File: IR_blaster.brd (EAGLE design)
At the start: 97.8 x 82.5 mm, 54 parts, among them J2 Micro USB, J3 Mini USB, J4 nRF24L01+, J5 FTDI, Q1IL1 BC337, Q1IL2 BC337, Q1IL3 BC337, Q1IL4 BC337, SW1P SPDT_SWITCH_2MM

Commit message: Changed the batteries packages to double pin ones.
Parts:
- BATT1, BATT2: device battery:CR2032H -> SparkFun-Batteries:BATTCOM_20MM_PTH
- moved R2IL4 6.35 mm to (2.54, 59.7)
- moved R1IL4 2.84 mm to (30.5, 52.7)
- moved Q1IL4 2.84 mm to (22.2, 52.7)
- moved R1BATT 1.80 mm to (45.7, 52.7)
- moved R2BATT 1.80 mm to (38.1, 52.7)
- moved BATT1 1.80 mm to (15.2, 68.6), turned to 90 degrees
- moved BATT2 1.27 mm to (38.1, 68.6), turned to 90 degrees
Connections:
- net GND: now also BATT1.2, BATT2.2; no longer BATT1.-, BATT2.-
- net V_BATT: now also BATT1.1, BATT2.1; no longer BATT1.+, BATT2.+
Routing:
- net N$15: track 9.94 -> 16.3 mm
- net 10: track 35.3 -> 39.0 mm
- net A0: track 14.4 -> 12.1 mm
- net N$14: track 33.2 -> 31.1 mm
- net V_BATT: track 109.3 -> 111.3 mm
- net N$16: track 8.67 -> 7.93 mm
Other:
- board text added: "revision 1.1"
- board text removed: "v"

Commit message: ...
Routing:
- net GND: track 18.2 -> 210.3 mm, vias 1 -> 8
- net CE: track 55.1 -> 61.4 mm
- net N$14: track 31.1 -> 36.3 mm
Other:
- board text removed: "revision 1.0"
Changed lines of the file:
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@@
 <wire x1="74.93" y1="10.16" x2="90.17" y2="10.16" width="0.254" layer="21"/>
 <wire x1="90.17" y1="10.16" x2="90.17" y2="38.1" width="0.254" layer="21"/>
-<text x="16.51" y="1.905" size="3.5" layer="1" font="vector">IR blaster</text>
-<text x="16.51" y="1.905" size="3.5" layer="31" font="vector">IR blaster</text>
-<text x="44.45" y="1.905" size="3.5" layer="16" font="vector" rot="MR0">IR blaster</text>
-<text x="32.385" y="5.08" size="1.27" layer="1" font="vector">revision 1.0</text>
-<text x="32.385" y="5.08" size="1.27" layer="31" font="vector">revision 1.1</text>
-<text x="28.575" y="5.08" size="1.27" layer="16" font="vector" rot="MR0">revision 1.1</text>
+<text x="17.78" y="2.54" size="3" layer="1" font="vector">IR blaster</text>
+<text x="17.78" y="2.54" size="3" layer="31" font="vector">IR blaster</text>
+<text x="41.91" y="2.54" size="3" layer="16" font="vector" rot="MR0">IR blaster</text>
+<text x="29.21" y="5.08" size="1.27" layer="1" font="vector">revision 1.1</text>
+<text x="29.21" y="5.08" size="1.27" layer="31" font="vector">revision 1.1</text>
+<text x="30.48" y="5.08" size="1.27" layer="16" font="vector" rot="MR0">revision 1.1</text>
 <text x="40.64" y="67.945" size="3.81" layer="16" font="vector" rot="MR0">Batteries</text>
 <text x="60.96" y="39.37" size="1.9304" layer="16" font="vector" rot="MR0">Microcontroller</text>
@@
 <text x="39.37" y="39.37" size="2.54" layer="31" font="vector">ATmega328</text>
 <text x="78.74" y="38.735" size="1.4224" layer="1" font="vector">nRF24L01+</text>
-<text x="22.86" y="59.69" size="1.778" layer="1" font="vector">CR2032</text>
-<text x="22.86" y="59.69" size="1.778" layer="31" font="vector">CR2032</text>
+<text x="22.225" y="58.42" size="1.778" layer="1" font="vector">CR2032</text>
+<text x="22.225" y="58.42" size="1.778" layer="31" font="vector">CR2032</text>
 <text x="22.225" y="34.29" size="1.4224" layer="31" font="vector">Restart</text>
 <text x="22.225" y="34.29" size="1.4224" layer="1" font="vector">Restart</text>
@@
 <via x="64.135" y="76.835" extent="1-16" drill="1" shape="square"/>
 <wire x1="64.135" y1="76.835" x2="66.04" y2="76.835" width="0.8128" layer="1"/>
+<wire x1="15.24" y1="60.43" x2="15.77" y2="60.43" width="1.27" layer="16"/>
+<wire x1="15.77" y1="60.43" x2="16.51" y2="59.69" width="1.27" layer="16"/>
+<wire x1="16.51" y1="59.69" x2="16.51" y2="55.88" width="1.27" layer="16"/>
+<wire x1="38.1" y1="60.43" x2="38.1" y2="56.515" width="1.27" layer="16"/>
+<wire x1="6.985" y1="46.99" x2="6.985" y2="48.26" width="0.8128" layer="16"/>
+<wire x1="6.985" y1="48.26" x2="7.62" y2="48.895" width="0.8128" layer="16"/>
+<wire x1="7.62" y1="48.895" x2="14.605" y2="48.895" width="0.8128" layer="16"/>
+<wire x1="14.605" y1="48.895" x2="16.51" y2="50.8" width="0.8128" layer="16"/>
+<wire x1="16.51" y1="50.8" x2="16.51" y2="55.88" width="0.8128" layer="16"/>
+<wire x1="22.225" y1="51.435" x2="17.145" y2="51.435" width="0.8128" layer="16"/>
+<wire x1="17.145" y1="51.435" x2="16.51" y2="50.8" width="0.8128" layer="16"/>
+<wire x1="6.985" y1="54.61" x2="6.985" y2="57.785" width="1.27" layer="16"/>
+<wire x1="6.985" y1="57.785" x2="9.525" y2="60.325" width="1.27" layer="16"/>
+<wire x1="9.525" y1="60.325" x2="15.135" y2="60.325" width="1.27" layer="16"/>
+<wire x1="15.135" y1="60.325" x2="15.24" y2="60.43" width="1.27" layer="16"/>
+<wire x1="59.055" y1="59.69" x2="59.055" y2="74.295" width="0.8128" layer="16"/>
+<wire x1="80.01" y1="64.77" x2="78.74" y2="64.77" width="0.8128" layer="16"/>
+<wire x1="78.74" y1="64.77" x2="77.47" y2="63.5" width="0.8128" layer="16"/>
+<wire x1="77.47" y1="63.5" x2="73.66" y2="63.5" width="0.8128" layer="16"/>
+<wire x1="73.66" y1="63.5" x2="71.12" y2="63.5" width="0.8128" layer="16"/>
+<via x="71.12" y="63.5" extent="1-16" drill="1" shape="square"/>
+<wire x1="72.39" y1="44.45" x2="74.93" y2="41.91" width="0.8128" layer="16"/>
+<wire x1="74.93" y1="41.91" x2="81.28" y2="41.91" width="0.8128" layer="16"/>
+<via x="81.28" y="41.91" extent="1-16" drill="1" shape="square"/>
+<wire x1="48.26" y1="44.45" x2="48.26" y2="46.99" width="0.8128" layer="16"/>
+<wire x1="48.26" y1="46.99" x2="59.055" y2="57.785" width="0.8128" layer="16"/>
+<wire x1="59.055" y1="57.785" x2="59.055" y2="59.69" width="0.8128" layer="16"/>
+<wire x1="50.8" y1="36.83" x2="50.8" y2="40.64" width="0.8128" layer="16"/>
+<wire x1="50.8" y1="40.64" x2="48.26" y2="43.18" width="0.8128" layer="16"/>
+<wire x1="48.26" y1="43.18" x2="48.26" y2="44.45" width="0.8128" layer="16"/>
+<wire x1="53.34" y1="22.86" x2="57.15" y2="22.86" width="0.8128" layer="16"/>
+<via x="57.15" y="22.86" extent="1-16" drill="1" shape="square"/>
+<wire x1="77.47" y1="11.43" x2="77.47" y2="6.35" width="0.8128" layer="16"/>
+<wire x1="88.9" y1="36.83" x2="92.075" y2="36.83" width="0.8128" layer="16"/>
+<wire x1="88.9" y1="36.83" x2="88.9" y2="38.1" width="0.8128" layer="16"/>
+<wire x1="88.9" y1="38.1" x2="90.805" y2="40.005" width="0.8128" layer="16"/>
+<via x="90.805" y="40.005" extent="1-16" drill="1" shape="square"/>
+<wire x1="90.805" y1="40.005" x2="90.805" y2="41.275" width="0.8128" layer="1"/>
+<wire x1="90.805" y1="41.275" x2="90.17" y2="41.91" width="0.8128" layer="1"/>
+<wire x1="90.17" y1="41.91" x2="81.28" y2="41.91" width="0.8128" layer="1"/>
+<wire x1="55.7784" y1="10.2108" x2="55.7784" y2="4.9784" width="0.8128" layer="16"/>
+<wire x1="55.7784" y1="4.9784" x2="53.34" y2="2.54" width="0.8128" layer="16"/>
+<wire x1="53.34" y1="2.54" x2="50.8" y2="2.54" width="0.8128" layer="16"/>
+<wire x1="43.2816" y1="10.2108" x2="38.1508" y2="10.2108" width="0.8128" layer="16"/>
+<wire x1="38.1508" y1="10.2108" x2="38.1" y2="10.16" width="0.8128" layer="16"/>
+<wire x1="55.7784" y1="10.2108" x2="58.3692" y2="10.2108" width="0.8128" layer="16"/>
+<wire x1="58.3692" y1="10.2108" x2="59.69" y2="8.89" width="0.8128" layer="16"/>
+<via x="38.1" y="10.16" extent="1-16" drill="1" shape="square"/>
+<via x="59.69" y="8.89" extent="1-16" drill="1" shape="square"/>
+<wire x1="17.78" y1="11.43" x2="22.86" y2="11.43" width="0.8128" layer="16"/>
+<via x="22.86" y="11.43" extent="1-16" drill="1" shape="square"/>
+<wire x1="6.35" y1="27.94" x2="4.445" y2="27.94" width="0.8128" layer="16"/>
+<wire x1="4.445" y1="27.94" x2="3.175" y2="26.67" width="0.8128" layer="16"/>
+<wire x1="3.175" y1="26.67" x2="3.175" y2="22.225" width="0.8128" layer="16"/>
+<wire x1="3.175" y1="22.225" x2="6.35" y2="19.05" width="0.8128" layer="16"/>
+<wire x1="6.35" y1="19.05" x2="8.89" y2="19.05" width="0.8128" layer="16"/>
+<wire x1="8.89" y1="19.05" x2="10.16" y2="20.32" width="0.8128" layer="16"/>
+<wire x1="10.16" y1="20.32" x2="13.97" y2="20.32" width="0.8128" layer="16"/>
+<wire x1="13.97" y1="20.32" x2="15.24" y2="19.05" width="0.8128" layer="16"/>
+<wire x1="15.24" y1="19.05" x2="15.24" y2="12.7" width="0.8128" layer="16"/>
+<wire x1="15.24" y1="12.7" x2="16.51" y2="11.43" width="0.8128" layer="16"/>
+<wire x1="16.51" y1="11.43" x2="17.78" y2="11.43" width="0.8128" layer="16"/>
 </signal>
 <signal name="V_BATT">
@@
 <contactref element="UC" pad="13"/>
 <contactref element="J4" pad="3"/>
-<wire x1="86.36" y1="36.83" x2="86.36" y2="38.1" width="0.8128" layer="16"/>
-<wire x1="86.36" y1="38.1" x2="87.63" y2="39.37" width="0.8128" layer="16"/>
-<wire x1="87.63" y1="39.37" x2="93.98" y2="39.37" width="0.8128" layer="16"/>
-<wire x1="93.98" y1="39.37" x2="95.25" y2="38.1" width="0.8128" layer="16"/>
-<wire x1="95.25" y1="38.1" x2="95.25" y2="33.02" width="0.8128" layer="16"/>
 <wire x1="95.25" y1="33.02" x2="93.98" y2="31.75" width="0.8128" layer="16"/>
 <wire x1="93.98" y1="31.75" x2="88.9" y2="31.75" width="0.8128" layer="16"/>
@@
 <wire x1="64.135" y1="34.925" x2="63.5" y2="35.56" width="0.8128" layer="16"/>
 <wire x1="63.5" y1="35.56" x2="63.5" y2="36.83" width="0.8128" layer="16"/>
+<wire x1="86.36" y1="36.83" x2="86.36" y2="41.275" width="0.8128" layer="16"/>
+<wire x1="86.36" y1="41.275" x2="87.63" y2="42.545" width="0.8128" layer="16"/>
+<wire x1="87.63" y1="42.545" x2="93.98" y2="42.545" width="0.8128" layer="16"/>
+<wire x1="93.98" y1="42.545" x2="95.25" y2="41.275" width="0.8128" layer="16"/>
+<wire x1="95.25" y1="41.275" x2="95.25" y2="33.02" width="0.8128" layer="16"/>
 </signal>
 <signal name="2">
@@
 <contactref element="IL4" pad="K"/>
 <wire x1="22.225" y1="53.975" x2="22.225" y2="60.324996875" width="1.27" layer="16"/>
-<wire x1="22.225" y1="60.324996875" x2="4.708025" y2="77.841971875" width="1.27" layer="16"/>
+<wire x1="4.708025" y1="77.841971875" x2="4.708025" y2="68.951975" width="0.8128" layer="16"/>
+<wire x1="4.708025" y1="68.951975" x2="8.89" y2="64.77" width="0.8128" layer="16"/>
+<wire x1="8.89" y1="64.77" x2="17.779996875" y2="64.77" width="0.8128" layer="16"/>
+<wire x1="17.779996875" y1="64.77" x2="22.225" y2="60.324996875" width="0.8128" layer="16"/>
 </signal>
 <signal name="N$15">
@@
 <wire x1="43.18" y1="15.2908" x2="43.2816" y2="15.1892" width="0.8128" layer="16"/>
 </signal>
+<signal name="N$3">
+</signal>
+<signal name="N$18">
+<via x="77.47" y="6.35" extent="1-16" drill="1" shape="square"/>
+</signal>
 </signals>

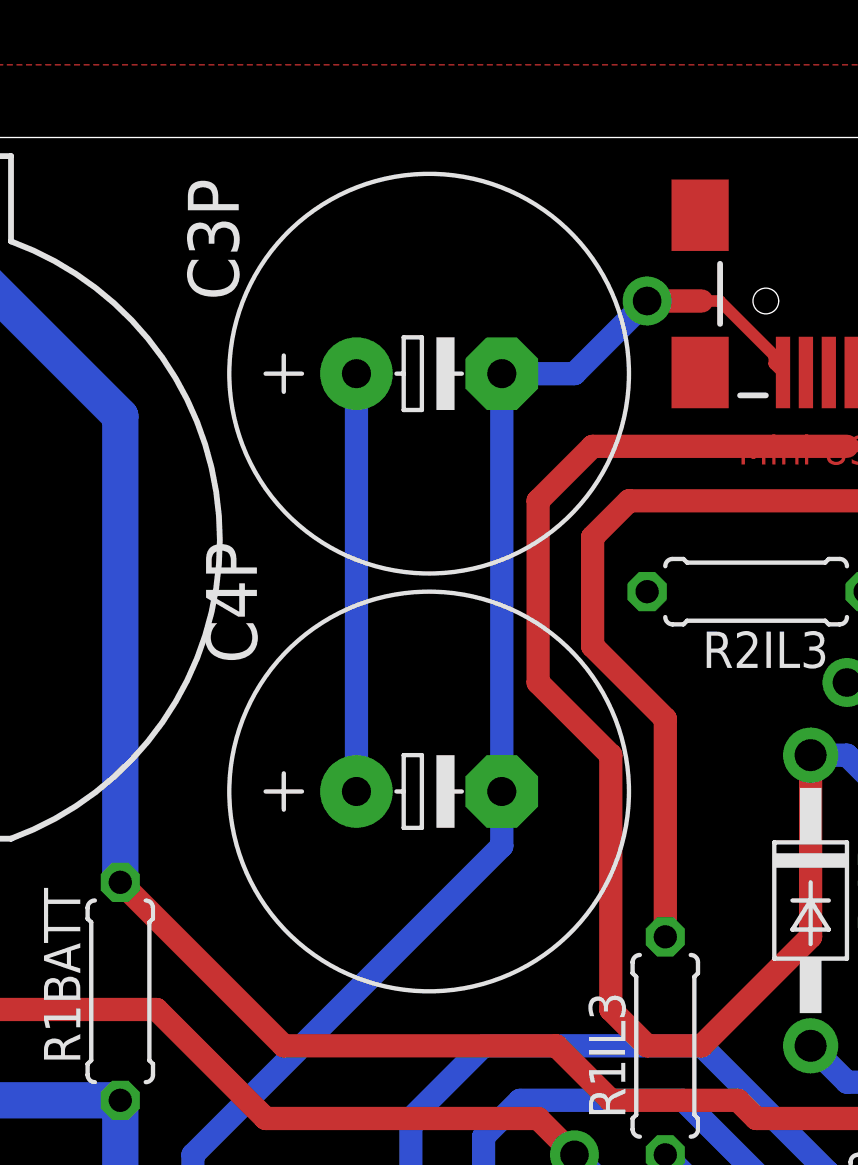
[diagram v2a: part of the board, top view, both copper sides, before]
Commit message: Changed to smaller capacitors
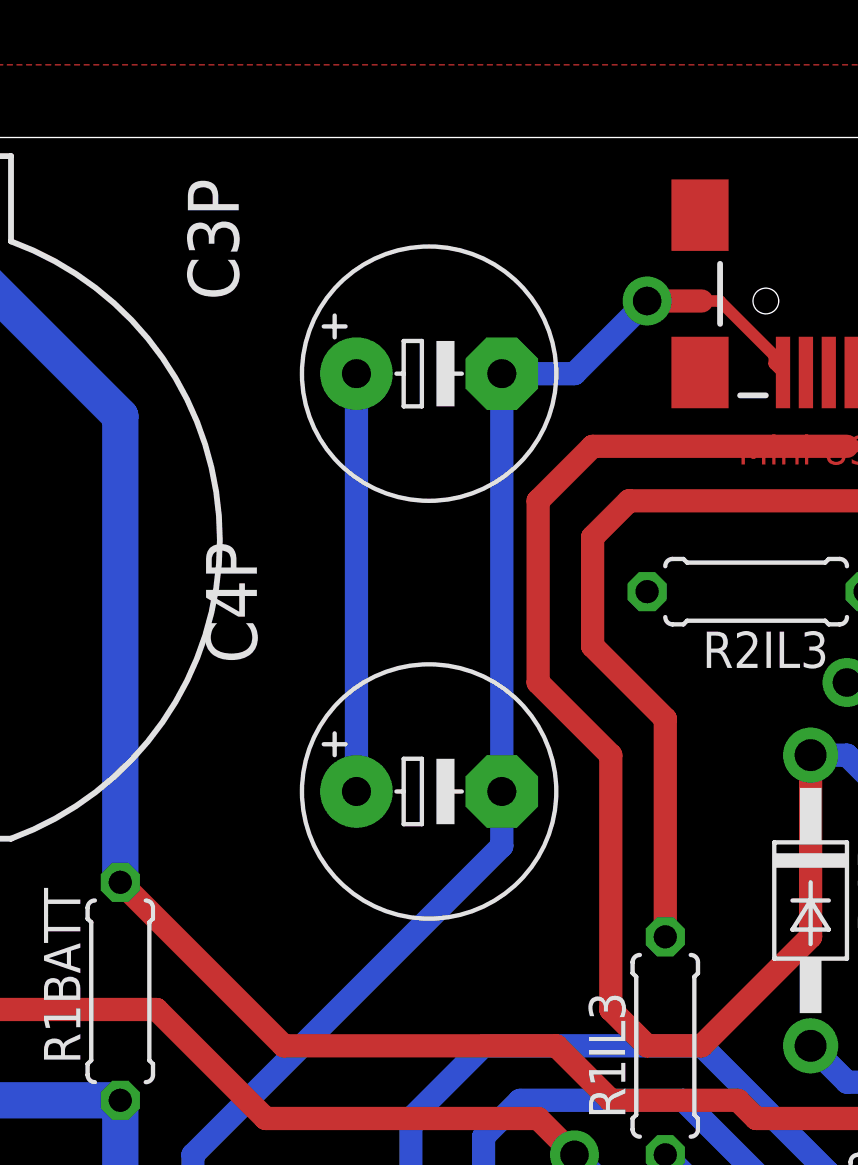
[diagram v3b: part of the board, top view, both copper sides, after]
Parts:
- C3P, C4P: value 3300u -> 470u; device resistor:E5-13 -> resistor:E5-8,5
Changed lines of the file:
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@@
 <attribute name="VALUE" x="83.8962" y="65.151" size="1.27" layer="27" ratio="10" rot="R270"/>
 </element>
-<element name="C3P" library="resistor" package="E5-13" value="3300u" x="56.515" y="74.295" smashed="yes">
+<element name="C3P" library="resistor" package="E5-8,5" value="470u" x="56.515" y="74.295" smashed="yes">
 <attribute name="NAME" x="49.8602" y="76.8604" size="1.778" layer="25" ratio="10" rot="R90"/>
 <attribute name="VALUE" x="51.943" y="70.358" size="1.778" layer="27" ratio="10"/>
@@
 <attribute name="VALUE" x="12.7" y="56.769" size="1.27" layer="27" ratio="10" rot="R180"/>
 </element>
-<element name="C4P" library="resistor" package="E5-13" value="3300u" x="56.515" y="59.69" smashed="yes">
+<element name="C4P" library="resistor" package="E5-8,5" value="470u" x="56.515" y="59.69" smashed="yes">
 <attribute name="NAME" x="50.4952" y="64.1604" size="1.778" layer="25" ratio="10" rot="R90"/>
 <attribute name="VALUE" x="51.943" y="55.753" size="1.778" layer="27" ratio="10"/>
